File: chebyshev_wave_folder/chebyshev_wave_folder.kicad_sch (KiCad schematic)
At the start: 62 parts, among them J1 Conn_01x02_Pin, J2 Conn_01x01_Pin, J3 Conn_01x01_Pin, J4 Conn_01x01_Pin, J5 Conn_01x01_Pin, Q1 PNP, Q10 NPN, Q4 NPN, Q5 PNP, Q6 NPN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

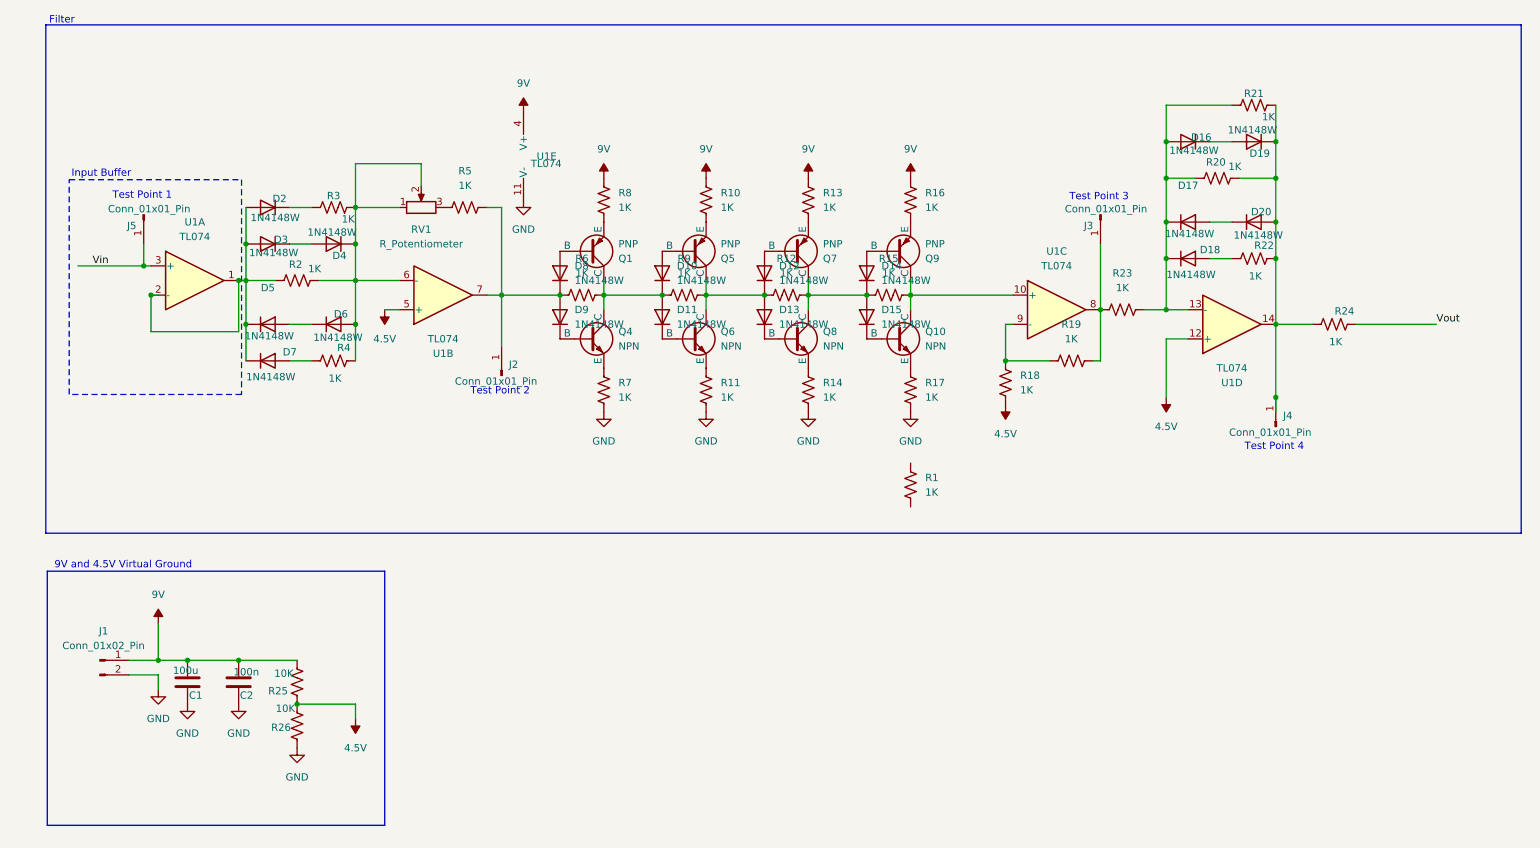
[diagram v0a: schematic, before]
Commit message: jfet buffer added
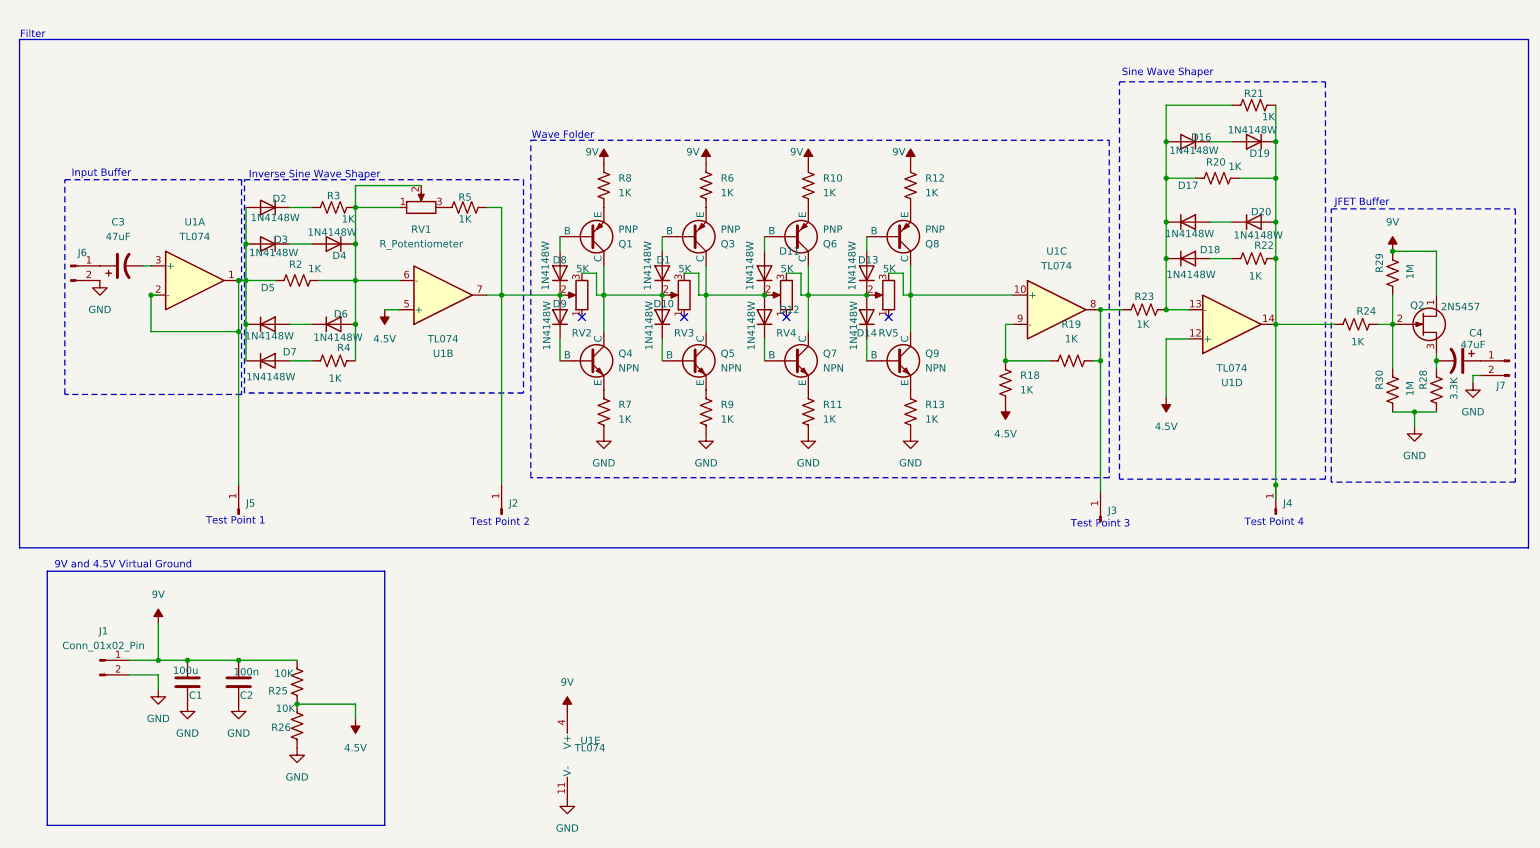
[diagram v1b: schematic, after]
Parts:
- removed D15: 1N4148W, Diode_SMD:D_SOD-123, symbol Diode:1N4148W
- removed Q10, Q6, Q8: NPN, Package_TO_SOT_SMD:SOT-23, symbol Simulation_SPICE:NPN
- removed Q5, Q7, Q9: PNP, Package_TO_SOT_SMD:SOT-23, symbol Simulation_SPICE:PNP
- removed R1, R14, R15, R16, R17: 1K, Resistor_SMD:R_1206_3216Metric, symbol Device:R_US
- added C3, C4: 47uF, Capacitor_THT:CP_Radial_D6.3mm_P2.50mm, symbol Device:C_Polarized_US
- added D1: 1N4148W, Diode_SMD:D_MiniMELF_Handsoldering, symbol Diode:1N4148W
- added J6, J7: Conn_01x02_Pin, Connector_PinHeader_2.54mm:PinHeader_1x02_P2.54mm_Vertical, symbol Connector:Conn_01x02_Pin
- added Q2: 2N5457, Package_TO_SOT_THT:TO-92, symbol Transistor_FET:2N3819
- added Q3, Q6, Q8: PNP, Package_TO_SOT_SMD:SOT-23, symbol Simulation_SPICE:PNP
- added Q5, Q7, Q9: NPN, Package_TO_SOT_SMD:SOT-23, symbol Simulation_SPICE:NPN
- added R28: 3.3K, Resistor_SMD:R_1206_3216Metric, symbol Device:R_US
- added R29, R30: 1M, Resistor_SMD:R_1206_3216Metric, symbol Device:R_US
- added RV2, RV3, RV4, RV5: 5K, Potentiometer_THT:Potentiometer_Runtron_RM-065_Vertical, symbol Device:R_Potentiometer
- C1, C2: footprint (none) -> Capacitor_SMD:C_1206_3216Metric_Pad1.33x1.80mm_HandSolder
- D10, D11, D12, D13, D14, D16, D17, D18, D19, D2, D20, D3, D4, D5, D6, D7, D8, D9: footprint Diode_SMD:D_SOD-123 -> Diode_SMD:D_MiniMELF_Handsoldering
- J1: footprint (none) -> Connector_PinHeader_2.54mm:PinHeader_1x02_P2.54mm_Vertical
- J2, J3, J4, J5: footprint (none) -> Connector_PinHeader_2.54mm:PinHeader_1x01_P2.54mm_Vertical
- RV1: footprint (none) -> Potentiometer_THT:Potentiometer_Runtron_RM-065_Vertical
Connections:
- net 9V: now also R12.1, R6.1, Q2.1 (D), R29.2; no longer R13.1
- net GND: now also R13.2, R9.2, J6.2 (Pin_2), J7.2 (Pin_2), R28.1, R30.1
- net at D2.2 (A), D3.2 (A), D5.1 (K)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: now also J5.1 (Pin_1)
- net at D10.2 (A): now also Q1.1 (C), Q4.1 (C), D1.1 (K), RV2.3, RV3.2
- net at D13.1 (K): now also D14.2 (A), Q6.1 (C), Q7.1 (C), RV4.3, RV5.2
- net at D8.1 (K), D9.2 (A), J2.1 (Pin_1)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: now also RV2.2; no longer R6.1
- net at D14.1 (K): now also Q9.2 (B); no longer R12.2
- net at D12.2 (A): now also D11.1 (K), Q3.1 (C), Q5.1 (C), RV3.3, RV4.2
- net at U1.10 (+): now also Q8.1 (C), Q9.1 (C), RV5.3
- net at R10.2: now also Q6.3 (E)
- net at R11.1: now also Q7.3 (E)
- net Vin: no longer names the net of U1.3 (+)
- net Vin: now also C3.2; no longer J5.1 (Pin_1)
- net Vout: no longer names the net of R24.2
- net Vout: now also Q2.2 (G), R29.1, R30.2
- new net: Q9.3 (E), R13.1
- new net: D1.2 (A), Q3.2 (B)
- new net: D10.1 (K), Q5.2 (B)
- new net: D13.2 (A), Q8.2 (B)
- new net: Q3.3 (E), R6.2
- new net: C4.2, Q2.3 (S), R28.2
- new net: C4.1, J7.1 (Pin_1)
- new net: Q8.3 (E), R12.2
- new net: Q5.3 (E), R9.1
- new net: D12.1 (K), Q7.2 (B)
- new net: C3.1, J6.1 (Pin_1)
- new net: D11.2 (A), Q6.2 (B)
- no-connect marks 0 -> 4
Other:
- note added: "Inverse Sine Wave Shaper"
- note added: "JFET Buffer"
- note added: "Sine Wave Shaper"
- note added: "Wave Folder"
- moved on the sheet: J2, J3, J4, J5, Q1, Q4, R23, R24, R7, R8, U1E

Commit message: updated schematic
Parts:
- removed C3: 47uF, Capacitor_THT:CP_Radial_D6.3mm_P2.50mm, symbol Device:C_Polarized_US
- removed D17, D19, D5: 1N4148W, Diode_SMD:D_MiniMELF_Handsoldering, symbol Diode:1N4148W
- removed R22, R24: 1K, Resistor_SMD:R_1206_3216Metric, symbol Device:R_US
- removed R29: 1M, Resistor_SMD:R_1206_3216Metric, symbol Device:R_US
- added C3: 100nF, Capacitor_SMD:C_1206_3216Metric_Pad1.33x1.80mm_HandSolder, symbol Device:C
- added C5: 22nF, Capacitor_SMD:C_1206_3216Metric_Pad1.33x1.80mm_HandSolder, symbol Device:C
- added R1: 1M, Resistor_SMD:R_1206_3216Metric, symbol Device:R_US
- added R14: 6.8K, Resistor_SMD:R_1206_3216Metric, symbol Device:R_US
- added R15, R16: 10K, Resistor_SMD:R_1206_3216Metric, symbol Device:R_US
- added RV6: 100K, Potentiometer_THT:Potentiometer_Runtron_RM-065_Vertical, symbol Device:R_Potentiometer
- C4: value 47uF -> 1uF
- D18, D2, D4: value 1N4148W -> SR240; footprint Diode_SMD:D_MiniMELF_Handsoldering -> Diode_SMD:D_SOD-123
- D7: value 1N4148W -> SR204; footprint Diode_SMD:D_MiniMELF_Handsoldering -> (none)
- Q1, Q3, Q6, Q8: value PNP -> 2N3906
- Q4, Q5, Q7, Q9: value NPN -> 2N3904
- R18, R21, R23, R3, R4: value 1K -> 10K
- R19: value 1K -> 22K
- R2: value 1K -> 3.3K
- R20: value 1K -> 8.2K
- R28: value 3.3K -> 10K
- RV1: value R_Potentiometer -> 20K
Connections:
- net 4.5V: now also R1.1, R15.1
- net GND: now also RV6.3
- net at D3.2 (A), D7.1 (K), J5.1 (Pin_1)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: now also R4.1, R14.2; no longer D2.2 (A), U1.2 (-)
- net at U1.3 (+): now also C3.1, R1.2
- net at D6.2 (A), R2.2, R3.2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: now also D2.1 (K); no longer D4.1 (K), R4.2, RV1.1
- net at Q2.2 (G), R30.2: now also C5.1
- net at D3.1 (K): now also D2.2 (A), R3.1; no longer D4.2 (A)
- net at D16.2 (A), D18.1 (K), R20.1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: now also R16.1; no longer R21.1
- net at D20.2 (A), J4.1 (Pin_1), R20.2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: now also D4.1 (K), C5.2
- net at D20.1 (K): now also D18.2 (A), R16.2
- net at D16.1 (K): now also D4.2 (A), R21.1
- net at Q2.3 (S), R28.2: now also C4.1; no longer C4.2
- net at J7.1 (Pin_1): now also RV6.2; no longer C4.1
- net at D6.1 (K): now also D7.2 (A), R4.2
- net at J6.1 (Pin_1): now also C3.2
- new net: R14.1, R15.2, U1.2 (-)
- new net: C4.2, RV6.1
- no-connect marks 4 -> 5
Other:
- note added: "External pot"
- moved on the sheet: C4, D2, J6, J7, Q2, R20, R21, R28, R30
